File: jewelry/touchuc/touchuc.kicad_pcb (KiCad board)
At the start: 2 copper layers, 8.4 x 21.2 mm, 19 parts, among them J1 Conn_01x01, J2 Conn_01x01, J3 Conn_01x01, J4 Conn_01x01, J5 Conn_01x01, J6 Conn_01x01, J7 Conn_01x01, J8 Conn_01x01, J9 Conn_01x01, U1 ATTINY10-TS

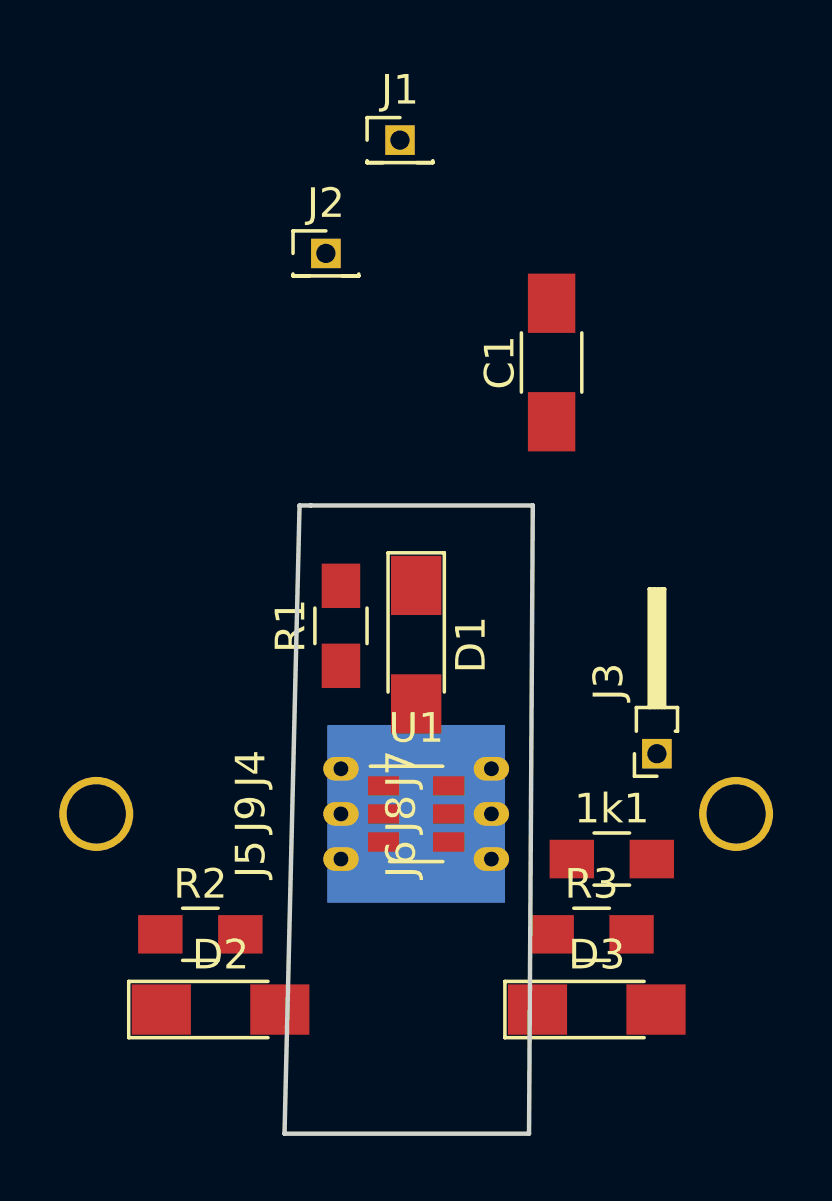
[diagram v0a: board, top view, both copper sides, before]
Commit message: jewelry: Minimize touchuC
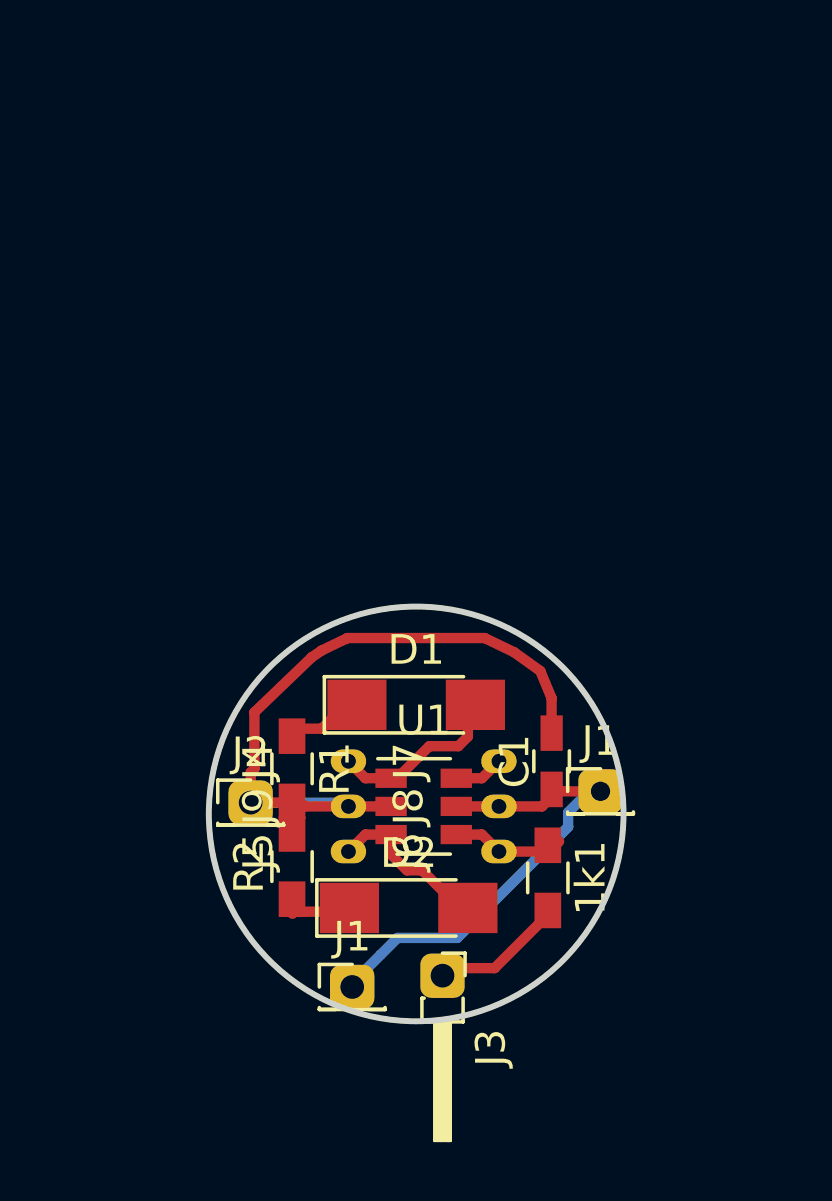
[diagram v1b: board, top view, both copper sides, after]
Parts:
- removed BT1: Battery_Cell, touchflower:BK-913
- removed D3: LED, LEDs:LED_1206_HandSoldering
- removed the J1 at (-0.55, -22.7)
- removed R3: R, Resistors_SMD:R_0805_HandSoldering
- added J1: Conn_01x01, Pin_Headers:Pin_Header_Straight_1x01_Pitch1.27mm, F.Cu at (-2.16, 5.84)
- added J1: Conn_01x01, Pin_Headers:Pin_Header_Straight_1x01_Pitch1.27mm, F.Cu at (6.22, -0.76)
- 1k1, R1, R2: footprint Resistors_SMD:R_0805_HandSoldering -> Resistors_SMD:R_0603_HandSoldering
- C1: footprint Capacitors_SMD:C_1206_HandSoldering -> Capacitors_SMD:C_0603_HandSoldering
- moved J2 18.7 mm to (-5.59, -0.38)
- moved C1 13.5 mm to (4.57, -1.78)
- moved J3 10.4 mm to (0.89, 5.46), turned to 270 degrees
- moved D2 7.22 mm to (-0.25, 3.17)
- moved R1 5.10 mm to (-4.19, -1.52), turned to 270 degrees
- moved R2 3.85 mm to (-4.19, 1.78), turned to 90 degrees
- moved 1k1 2.25 mm to (4.45, 2.16), turned to 270 degrees
- moved D1 2.03 mm to (0.00, -3.68), turned to 0 degrees
- moved J4 0.36 mm to (-2.29, -1.78)
- moved J5 0.36 mm to (-2.29, 1.27)
- moved J6 0.36 mm to (2.79, 1.27)
- moved J7 0.36 mm to (2.79, -1.78)
- moved J8 0.36 mm to (2.79, -0.25)
- moved J9 0.36 mm to (-2.29, -0.25)
- moved U1 0.36 mm to (0.25, -0.25)
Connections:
- net LED3 renamed /reset
- J9 pad 1: Net-(J9-Pad1) -> -BATT
- U1 pad 2: Net-(J9-Pad1) -> -BATT
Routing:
- net -BATT: track 0.00 -> 26.1 mm
- net +BATT: track 0.00 -> 16.0 mm
- net LED1: track 0.00 -> 6.05 mm
- net LED2: track 0.00 -> 5.74 mm
- net /sense: track 0.00 -> 4.45 mm
- net TOUCH: track 0.00 -> 3.85 mm
- net Net-(D1-Pad1): track 0.00 -> 2.32 mm
- net Net-(D2-Pad1): track 0.00 -> 1.95 mm
- net /reset: track 0.00 -> 1.68 mm
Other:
- board size 8.4 x 21.2 mm -> 14 x 14 mm

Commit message: jewelry: Update TODO
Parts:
- moved J1 0.13 mm to (-2.16, 5.71)
- moved J1 0.13 mm to (6.10, -0.76)
- moved R1 0.13 mm to (-4.06, -1.52)
- moved R2 0.13 mm to (-4.06, 1.78)
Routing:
- net -BATT: track 26.1 -> 25.4 mm
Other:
- board size 14 x 14 mm -> 13 x 13 mm
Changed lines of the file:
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@@
   )
   (module Pin_Headers:Pin_Header_Straight_1x01_Pitch1.27mm (layer F.Cu)
-    (at -2.159 5.842)
+    (at -2.159 5.715)
     (descr "Through hole straight pin header, 1x01, 1.27mm pitch, single row")
     (tags "Through hole pin header THT 1x01 1.27mm single row")
@@
   )
   (module Resistors_SMD:R_0603_HandSoldering (layer F.Cu)
-    (at -4.191 -1.524 270)
+    (at -4.064 -1.524 270)
     (descr "Resistor SMD 0603, hand soldering")
     (tags "resistor 0603")
@@
   )
   (module Resistors_SMD:R_0603_HandSoldering (layer F.Cu)
-    (at -4.191 1.778 90)
+    (at -4.064 1.778 90)
     (descr "Resistor SMD 0603, hand soldering")
     (tags "resistor 0603")
@@
   )
   (module Pin_Headers:Pin_Header_Straight_1x01_Pitch1.27mm (layer F.Cu)
-    (at 6.223 -0.762)
+    (at 6.096 -0.762)
     (descr "Through hole straight pin header, 1x01, 1.27mm pitch, single row")
     (tags "Through hole pin header THT 1x01 1.27mm single row")
@@
   )
   (gr_circle (center 0 0) (end 10 0) (layer Eco2.User) (width 0.2))
-  (gr_circle (center 0 0) (end 7 0) (layer Edge.Cuts) (width 0.2))
+  (gr_circle (center 0 0) (end 6.5 0) (layer Edge.Cuts) (width 0.2))
   (segment (start -1.712 -1.204) (end -2.286 -1.778) (width 0.35) (layer F.Cu) (net 1))
   (segment (start -0.846 -1.204) (end -1.712 -1.204) (width 0.35) (layer F.Cu) (net 1))
@@
   (segment (start -5.588 -0.381) (end -4.234 -0.381) (width 0.35) (layer F.Cu) (net 6))
   (segment (start -4.191 -0.424) (end -4.191 -0.574) (width 0.35) (layer F.Cu) (net 6))
-  (segment (start -5.588 -1.397) (end -5.588 -0.381) (width 0.35) (layer F.Cu) (net 6))
-  (segment (start -5.461 -1.524) (end -5.588 -1.397) (width 0.35) (layer F.Cu) (net 6))
-  (segment (start 4.572 -3.906002) (end 4.191 -4.826) (width 0.35) (layer F.Cu) (net 6))
-  (segment (start 4.572 -2.728) (end 4.572 -3.906002) (width 0.35) (layer F.Cu) (net 6))
-  (segment (start -2.328401 -5.932682) (end -3.186615 -5.519388) (width 0.35) (layer F.Cu) (net 6))
-  (segment (start -2.312377 -5.937624) (end -2.328401 -5.932682) (width 0.35) (layer F.Cu) (net 6))
-  (segment (start -5.461 -3.429) (end -5.461 -1.524) (width 0.35) (layer F.Cu) (net 6))
-  (segment (start -3.525069 -5.288635) (end -5.461 -3.429) (width 0.35) (layer F.Cu) (net 6))
-  (segment (start 4.191 -4.826) (end 3.302 -5.461) (width 0.35) (layer F.Cu) (net 6))
-  (segment (start 3.302 -5.461) (end 2.312376 -5.937624) (width 0.35) (layer F.Cu) (net 6))
-  (segment (start -3.186615 -5.519388) (end -3.525069 -5.288635) (width 0.35) (layer F.Cu) (net 6))
-  (segment (start 2.312376 -5.937624) (end -2.312377 -5.937624) (width 0.35) (layer F.Cu) (net 6))
   (segment (start -2.413 -0.381) (end -2.286 -0.254) (width 0.35) (layer B.Cu) (net 6))
   (segment (start -5.588 -0.381) (end -2.413 -0.381) (width 0.35) (layer B.Cu) (net 6))
+  (segment (start -5.461 -1.524) (end -5.588 -1.397) (width 0.35) (layer F.Cu) (net 6))
+  (segment (start -3.556 -5.08) (end -4.953 -3.81) (width 0.35) (layer F.Cu) (net 6))
+  (segment (start -3.175 -5.334) (end -3.556 -5.08) (width 0.35) (layer F.Cu) (net 6))
+  (segment (start 4.572 -3.906002) (end 4.318 -4.318) (width 0.35) (layer F.Cu) (net 6))
+  (segment (start -4.953 -3.81) (end -5.461 -1.524) (width 0.35) (layer F.Cu) (net 6))
+  (segment (start 4.572 -2.728) (end 4.572 -3.906002) (width 0.35) (layer F.Cu) (net 6))
+  (segment (start -2.286 -5.588) (end -3.175 -5.334) (width 0.35) (layer F.Cu) (net 6))
+  (segment (start 3.937 -4.699) (end 2.667 -5.461) (width 0.35) (layer F.Cu) (net 6))
+  (segment (start 2.159 -5.715) (end -2.286 -5.588) (width 0.35) (layer F.Cu) (net 6))
+  (segment (start -5.588 -1.397) (end -5.588 -0.381) (width 0.35) (layer F.Cu) (net 6))
+  (segment (start 4.318 -4.318) (end 3.937 -4.699) (width 0.35) (layer F.Cu) (net 6))
+  (segment (start 2.667 -5.461) (end 2.159 -5.715) (width 0.35) (layer F.Cu) (net 6))
   (segment (start -3.186 -2.878) (end -2.254 -3.81) (width 0.35) (layer F.Cu) (net 7))
   (segment (start -4.191 -2.878) (end -3.186 -2.878) (width 0.35) (layer F.Cu) (net 7))
